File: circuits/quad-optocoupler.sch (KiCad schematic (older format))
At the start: 6 parts, among them U3 TLP291-4

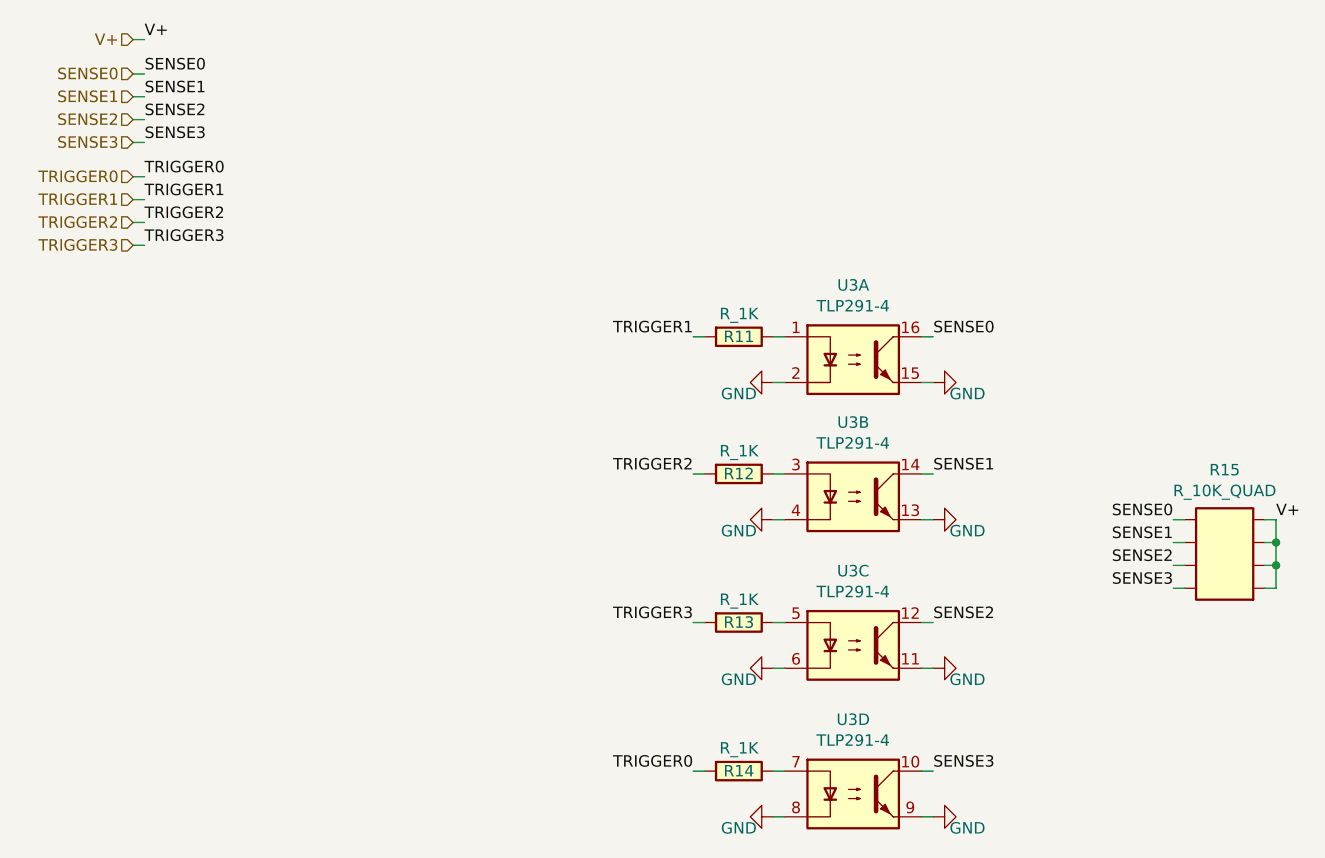
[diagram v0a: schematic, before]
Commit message: changed footprint for 0402 resistor array, sent back to fab
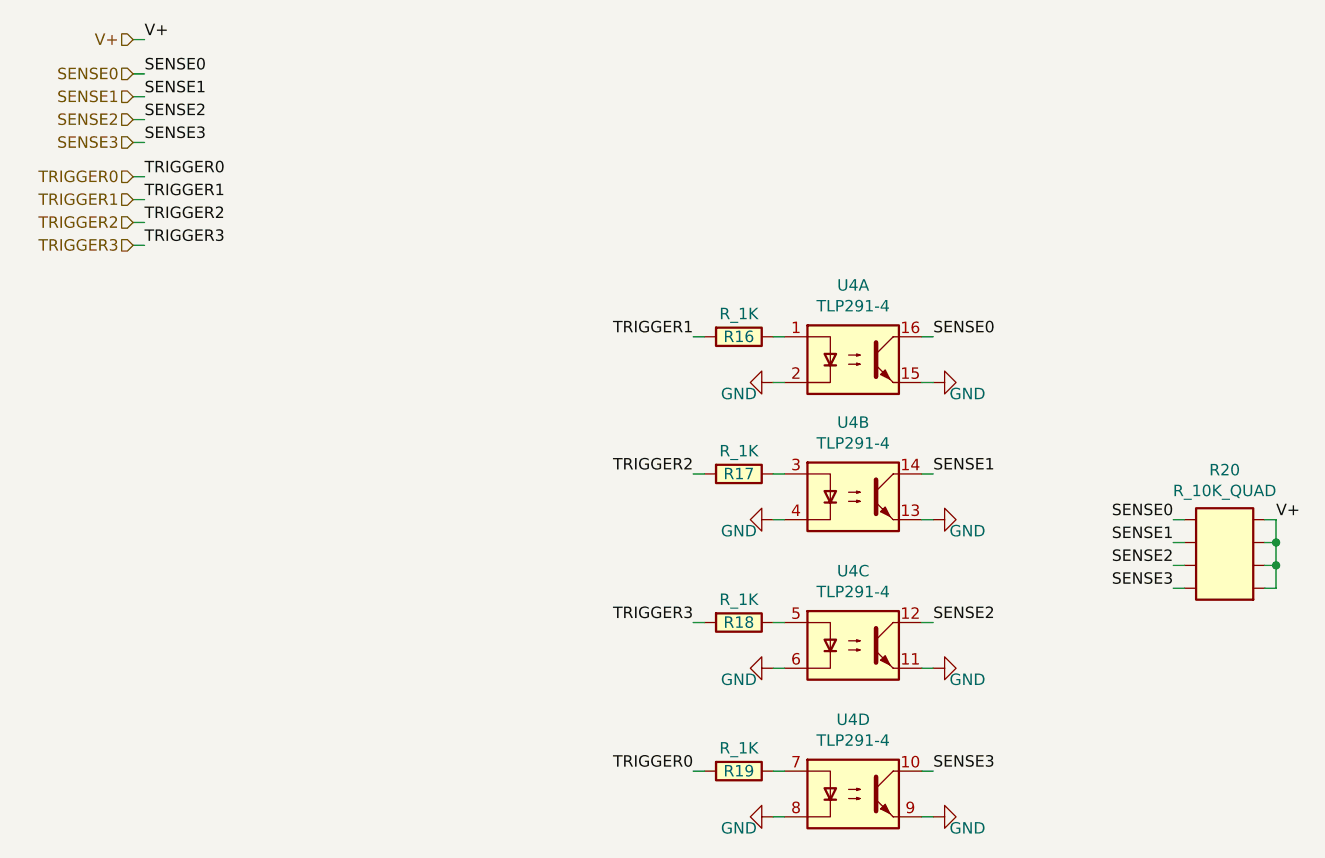
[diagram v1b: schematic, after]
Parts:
- R15: footprint Open_Automation:R_0402_1005Metric_Quad -> Resistor_SMD:R_Array_Concave_4x0402
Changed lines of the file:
@@
 $Descr A4 11693 8268
 encoding utf-8
-Sheet 4 12
+Sheet 5 12
 Title ""
 Date ""
@@
 AR Path="/601A4F03/5FDDC68F" Ref="U5"  Part="1"
 AR Path="/6021992A/5FDDC68F" Ref="U6"  Part="1"
-F 0 "U3" H 4350 2525 50  0000 C CNN
+F 0 "U4" H 4350 2525 50  0000 C CNN
 F 1 "TLP291-4" H 4350 2434 50  0000 C CNN
 F 2 "Package_SO:SOP-16_4.4x10.4mm_P1.27mm" H 4150 2000 50  0001 L CIN
@@
 AR Path="/601A4F03/5FDDC695" Ref="U5"  Part="2"
 AR Path="/6021992A/5FDDC695" Ref="U6"  Part="2"
-F 0 "U3" H 4350 3125 50  0000 C CNN
+F 0 "U4" H 4350 3125 50  0000 C CNN
 F 1 "TLP291-4" H 4350 3034 50  0000 C CNN
 F 2 "Package_SO:SOP-16_4.4x10.4mm_P1.27mm" H 4150 2600 50  0001 L CIN
@@
 AR Path="/601A4F03/5FDDC69B" Ref="U5"  Part="3"
 AR Path="/6021992A/5FDDC69B" Ref="U6"  Part="3"
-F 0 "U3" H 4350 3775 50  0000 C CNN
+F 0 "U4" H 4350 3775 50  0000 C CNN
 F 1 "TLP291-4" H 4350 3684 50  0000 C CNN
 F 2 "Package_SO:SOP-16_4.4x10.4mm_P1.27mm" H 4150 3250 50  0001 L CIN
@@
 AR Path="/601A4F03/5FDDC6A1" Ref="U5"  Part="4"
 AR Path="/6021992A/5FDDC6A1" Ref="U6"  Part="4"
-F 0 "U3" H 4350 4425 50  0000 C CNN
+F 0 "U4" H 4350 4425 50  0000 C CNN
 F 1 "TLP291-4" H 4350 4334 50  0000 C CNN
 F 2 "Package_SO:SOP-16_4.4x10.4mm_P1.27mm" H 4150 3900 50  0001 L CIN
@@
 AR Path="/601A4F03/5FF8C5A1" Ref="R25"  Part="1"
 AR Path="/6021992A/5FF8C5A1" Ref="R30"  Part="1"
-F 0 "R15" H 5975 3517 50  0000 C CNN
+F 0 "R20" H 5975 3517 50  0000 C CNN
 F 1 "R_10K_QUAD" H 5975 3426 50  0000 C CNN
-F 2 "Open_Automation:R_0402_1005Metric_Quad" H 6200 2500 50  0001 C CNN
+F 2 "Resistor_SMD:R_Array_Concave_4x0402" H 6200 2500 50  0001 C CNN
 F 3 "https://datasheet.lcsc.com/szlcsc/Uniroyal-Elec-4D02WGJ0103TCE_C25725.pdf" H 6200 2720 50  0001 C CNN
 F 4 "4D02WGJ0103TCE" H 6250 2670 60  0001 C CNN "Part Number"
@@
 AR Path="/601130DF/5FDC968D" Ref="#PWR042"  Part="1"
 AR Path="/6021992A/5FDC968D" Ref="#PWR058"  Part="1"
-F 0 "#PWR034" H 4700 2050 50  0001 C CNN
+F 0 "#PWR058" H 4700 2050 50  0001 C CNN
 F 1 "GND" V 4650 2150 50  0000 C CNN
 F 2 "" H 4700 2300 50  0001 C CNN
@@
 AR Path="/601130DF/5FDCB365" Ref="#PWR043"  Part="1"
 AR Path="/6021992A/5FDCB365" Ref="#PWR059"  Part="1"
-F 0 "#PWR035" H 4700 2650 50  0001 C CNN
+F 0 "#PWR059" H 4700 2650 50  0001 C CNN
 F 1 "GND" V 4650 2750 50  0000 C CNN
 F 2 "" H 4700 2900 50  0001 C CNN
@@
 AR Path="/601130DF/5FDCD5D6" Ref="#PWR044"  Part="1"
 AR Path="/6021992A/5FDCD5D6" Ref="#PWR060"  Part="1"
-F 0 "#PWR036" H 4700 3300 50  0001 C CNN
+F 0 "#PWR060" H 4700 3300 50  0001 C CNN
 F 1 "GND" V 4650 3400 50  0000 C CNN
 F 2 "" H 4700 3550 50  0001 C CNN
@@
 AR Path="/601130DF/5FDD131C" Ref="#PWR045"  Part="1"
 AR Path="/6021992A/5FDD131C" Ref="#PWR061"  Part="1"
-F 0 "#PWR037" H 4700 3950 50  0001 C CNN
+F 0 "#PWR061" H 4700 3950 50  0001 C CNN
 F 1 "GND" V 4650 4050 50  0000 C CNN
 F 2 "" H 4700 4200 50  0001 C CNN
@@
 AR Path="/601130DF/5FDD4573" Ref="#PWR041"  Part="1"
 AR Path="/6021992A/5FDD4573" Ref="#PWR057"  Part="1"
-F 0 "#PWR033" H 4000 3950 50  0001 C CNN
+F 0 "#PWR057" H 4000 3950 50  0001 C CNN
 F 1 "GND" V 4050 4050 50  0000 C CNN
 F 2 "" H 4000 4200 50  0001 C CNN
@@
 AR Path="/601130DF/5FDD7FBA" Ref="#PWR040"  Part="1"
 AR Path="/6021992A/5FDD7FBA" Ref="#PWR056"  Part="1"
-F 0 "#PWR032" H 4000 3300 50  0001 C CNN
+F 0 "#PWR056" H 4000 3300 50  0001 C CNN
 F 1 "GND" V 4050 3400 50  0000 C CNN
 F 2 "" H 4000 3550 50  0001 C CNN
@@
 AR Path="/601130DF/5FDDBD71" Ref="#PWR039"  Part="1"
 AR Path="/6021992A/5FDDBD71" Ref="#PWR055"  Part="1"
-F 0 "#PWR031" H 4000 2650 50  0001 C CNN
+F 0 "#PWR055" H 4000 2650 50  0001 C CNN
 F 1 "GND" V 4050 2750 50  0000 C CNN
 F 2 "" H 4000 2900 50  0001 C CNN
@@
 AR Path="/601130DF/5FDDF0DF" Ref="#PWR038"  Part="1"
 AR Path="/6021992A/5FDDF0DF" Ref="#PWR054"  Part="1"
-F 0 "#PWR030" H 4000 2050 50  0001 C CNN
+F 0 "#PWR054" H 4000 2050 50  0001 C CNN
 F 1 "GND" V 4050 2150 50  0000 C CNN
 F 2 "" H 4000 2300 50  0001 C CNN
@@
 AR Path="/601A4F03/5FDD0A2D" Ref="R21"  Part="1"
 AR Path="/6021992A/5FDD0A2D" Ref="R26"  Part="1"
-F 0 "R11" V 3850 2100 50  0000 C CNN
+F 0 "R16" V 3850 2100 50  0000 C CNN
 F 1 "R_1K" V 3750 2100 50  0000 C CNN
 F 2 "Resistor_SMD:R_0603_1608Metric_Pad0.98x0.95mm_HandSolder" V 3780 2100 50  0001 C CNN
@@
 AR Path="/601A4F03/5FDD4F3C" Ref="R22"  Part="1"
 AR Path="/6021992A/5FDD4F3C" Ref="R27"  Part="1"
-F 0 "R12" V 3850 2700 50  0000 C CNN
+F 0 "R17" V 3850 2700 50  0000 C CNN
 F 1 "R_1K" V 3750 2700 50  0000 C CNN
 F 2 "Resistor_SMD:R_0603_1608Metric_Pad0.98x0.95mm_HandSolder" V 3780 2700 50  0001 C CNN
@@
 AR Path="/601A4F03/5FDDB0BD" Ref="R23"  Part="1"
 AR Path="/6021992A/5FDDB0BD" Ref="R28"  Part="1"
-F 0 "R13" V 3850 3350 50  0000 C CNN
+F 0 "R18" V 3850 3350 50  0000 C CNN
 F 1 "R_1K" V 3750 3350 50  0000 C CNN
 F 2 "Resistor_SMD:R_0603_1608Metric_Pad0.98x0.95mm_HandSolder" V 3780 3350 50  0001 C CNN
@@
 AR Path="/601A4F03/5FDDEE05" Ref="R24"  Part="1"
 AR Path="/6021992A/5FDDEE05" Ref="R29"  Part="1"
-F 0 "R14" V 3850 4000 50  0000 C CNN
+F 0 "R19" V 3850 4000 50  0000 C CNN
 F 1 "R_1K" V 3750 4000 50  0000 C CNN
 F 2 "Resistor_SMD:R_0603_1608Metric_Pad0.98x0.95mm_HandSolder" V 3780 4000 50  0001 C CNN

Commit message: finished schematic corrections, working on layout
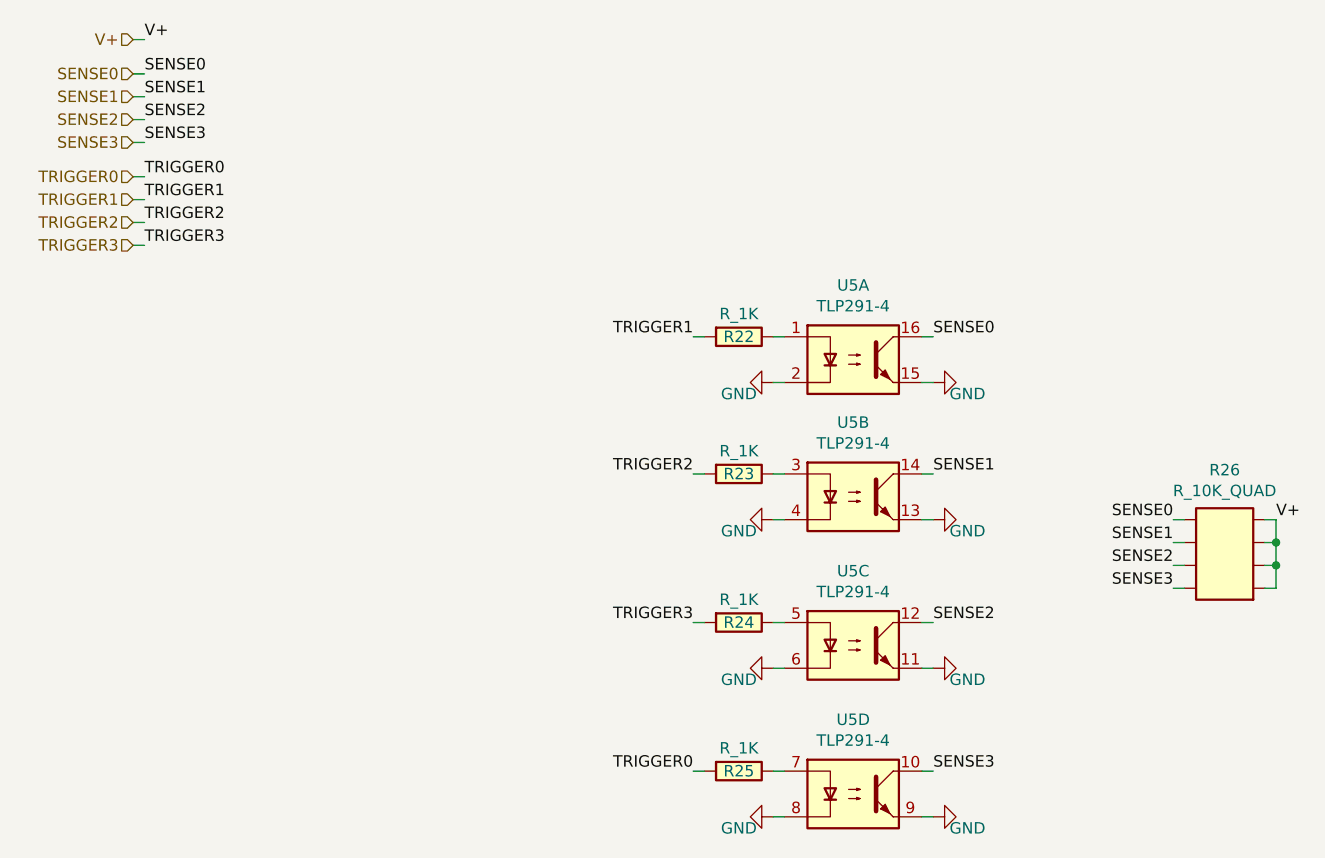
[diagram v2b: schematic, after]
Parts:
- renumbered R11 to R12, R12 to R13, R13 to R14, R14 to R15, R15 to R16

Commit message: finished layout, sent to board house
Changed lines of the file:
@@
 $Descr A4 11693 8268
 encoding utf-8
-Sheet 6 12
+Sheet 7 12
 Title ""
 Date ""
@@
 AR Path="/601A4F03/5FDDC68F" Ref="U5"  Part="1"
 AR Path="/6021992A/5FDDC68F" Ref="U6"  Part="1"
-F 0 "U5" H 4350 2525 50  0000 C CNN
+F 0 "U6" H 4350 2525 50  0000 C CNN
 F 1 "TLP291-4" H 4350 2434 50  0000 C CNN
 F 2 "Package_SO:SOP-16_4.4x10.4mm_P1.27mm" H 4150 2000 50  0001 L CIN
@@
 AR Path="/601A4F03/5FDDC695" Ref="U5"  Part="2"
 AR Path="/6021992A/5FDDC695" Ref="U6"  Part="2"
-F 0 "U5" H 4350 3125 50  0000 C CNN
+F 0 "U6" H 4350 3125 50  0000 C CNN
 F 1 "TLP291-4" H 4350 3034 50  0000 C CNN
 F 2 "Package_SO:SOP-16_4.4x10.4mm_P1.27mm" H 4150 2600 50  0001 L CIN
@@
 AR Path="/601A4F03/5FDDC69B" Ref="U5"  Part="3"
 AR Path="/6021992A/5FDDC69B" Ref="U6"  Part="3"
-F 0 "U5" H 4350 3775 50  0000 C CNN
+F 0 "U6" H 4350 3775 50  0000 C CNN
 F 1 "TLP291-4" H 4350 3684 50  0000 C CNN
 F 2 "Package_SO:SOP-16_4.4x10.4mm_P1.27mm" H 4150 3250 50  0001 L CIN
@@
 AR Path="/601A4F03/5FDDC6A1" Ref="U5"  Part="4"
 AR Path="/6021992A/5FDDC6A1" Ref="U6"  Part="4"
-F 0 "U5" H 4350 4425 50  0000 C CNN
+F 0 "U6" H 4350 4425 50  0000 C CNN
 F 1 "TLP291-4" H 4350 4334 50  0000 C CNN
 F 2 "Package_SO:SOP-16_4.4x10.4mm_P1.27mm" H 4150 3900 50  0001 L CIN
@@
 AR Path="/601A4F03/5FF8C5A1" Ref="R26"  Part="1"
 AR Path="/6021992A/5FF8C5A1" Ref="R31"  Part="1"
-F 0 "R26" H 5975 3517 50  0000 C CNN
+F 0 "R31" H 5975 3517 50  0000 C CNN
 F 1 "R_10K_QUAD" H 5975 3426 50  0000 C CNN
 F 2 "Resistor_SMD:R_Array_Concave_4x0402" H 6200 2500 50  0001 C CNN
@@
 AR Path="/601130DF/5FDC968D" Ref="#PWR041"  Part="1"
 AR Path="/6021992A/5FDC968D" Ref="#PWR057"  Part="1"
-F 0 "#PWR049" H 4700 2050 50  0001 C CNN
+F 0 "#PWR057" H 4700 2050 50  0001 C CNN
 F 1 "GND" V 4650 2150 50  0000 C CNN
 F 2 "" H 4700 2300 50  0001 C CNN
@@
 AR Path="/601130DF/5FDCB365" Ref="#PWR042"  Part="1"
 AR Path="/6021992A/5FDCB365" Ref="#PWR058"  Part="1"
-F 0 "#PWR050" H 4700 2650 50  0001 C CNN
+F 0 "#PWR058" H 4700 2650 50  0001 C CNN
 F 1 "GND" V 4650 2750 50  0000 C CNN
 F 2 "" H 4700 2900 50  0001 C CNN
@@
 AR Path="/601130DF/5FDCD5D6" Ref="#PWR043"  Part="1"
 AR Path="/6021992A/5FDCD5D6" Ref="#PWR059"  Part="1"
-F 0 "#PWR051" H 4700 3300 50  0001 C CNN
+F 0 "#PWR059" H 4700 3300 50  0001 C CNN
 F 1 "GND" V 4650 3400 50  0000 C CNN
 F 2 "" H 4700 3550 50  0001 C CNN
@@
 AR Path="/601130DF/5FDD131C" Ref="#PWR044"  Part="1"
 AR Path="/6021992A/5FDD131C" Ref="#PWR060"  Part="1"
-F 0 "#PWR052" H 4700 3950 50  0001 C CNN
+F 0 "#PWR060" H 4700 3950 50  0001 C CNN
 F 1 "GND" V 4650 4050 50  0000 C CNN
 F 2 "" H 4700 4200 50  0001 C CNN
@@
 AR Path="/601130DF/5FDD4573" Ref="#PWR040"  Part="1"
 AR Path="/6021992A/5FDD4573" Ref="#PWR056"  Part="1"
-F 0 "#PWR048" H 4000 3950 50  0001 C CNN
+F 0 "#PWR056" H 4000 3950 50  0001 C CNN
 F 1 "GND" V 4050 4050 50  0000 C CNN
 F 2 "" H 4000 4200 50  0001 C CNN
@@
 AR Path="/601130DF/5FDD7FBA" Ref="#PWR039"  Part="1"
 AR Path="/6021992A/5FDD7FBA" Ref="#PWR055"  Part="1"
-F 0 "#PWR047" H 4000 3300 50  0001 C CNN
+F 0 "#PWR055" H 4000 3300 50  0001 C CNN
 F 1 "GND" V 4050 3400 50  0000 C CNN
 F 2 "" H 4000 3550 50  0001 C CNN
@@
 AR Path="/601130DF/5FDDBD71" Ref="#PWR038"  Part="1"
 AR Path="/6021992A/5FDDBD71" Ref="#PWR054"  Part="1"
-F 0 "#PWR046" H 4000 2650 50  0001 C CNN
+F 0 "#PWR054" H 4000 2650 50  0001 C CNN
 F 1 "GND" V 4050 2750 50  0000 C CNN
 F 2 "" H 4000 2900 50  0001 C CNN
@@
 AR Path="/601130DF/5FDDF0DF" Ref="#PWR037"  Part="1"
 AR Path="/6021992A/5FDDF0DF" Ref="#PWR053"  Part="1"
-F 0 "#PWR045" H 4000 2050 50  0001 C CNN
+F 0 "#PWR053" H 4000 2050 50  0001 C CNN
 F 1 "GND" V 4050 2150 50  0000 C CNN
 F 2 "" H 4000 2300 50  0001 C CNN
@@
 AR Path="/601A4F03/5FDD0A2D" Ref="R22"  Part="1"
 AR Path="/6021992A/5FDD0A2D" Ref="R27"  Part="1"
-F 0 "R22" V 3850 2100 50  0000 C CNN
+F 0 "R27" V 3850 2100 50  0000 C CNN
 F 1 "R_1K" V 3750 2100 50  0000 C CNN
 F 2 "Resistor_SMD:R_0603_1608Metric_Pad0.98x0.95mm_HandSolder" V 3780 2100 50  0001 C CNN
@@
 AR Path="/601A4F03/5FDD4F3C" Ref="R23"  Part="1"
 AR Path="/6021992A/5FDD4F3C" Ref="R28"  Part="1"
-F 0 "R23" V 3850 2700 50  0000 C CNN
+F 0 "R28" V 3850 2700 50  0000 C CNN
 F 1 "R_1K" V 3750 2700 50  0000 C CNN
 F 2 "Resistor_SMD:R_0603_1608Metric_Pad0.98x0.95mm_HandSolder" V 3780 2700 50  0001 C CNN
@@
 AR Path="/601A4F03/5FDDB0BD" Ref="R24"  Part="1"
 AR Path="/6021992A/5FDDB0BD" Ref="R29"  Part="1"
-F 0 "R24" V 3850 3350 50  0000 C CNN
+F 0 "R29" V 3850 3350 50  0000 C CNN
 F 1 "R_1K" V 3750 3350 50  0000 C CNN
 F 2 "Resistor_SMD:R_0603_1608Metric_Pad0.98x0.95mm_HandSolder" V 3780 3350 50  0001 C CNN
@@
 AR Path="/601A4F03/5FDDEE05" Ref="R25"  Part="1"
 AR Path="/6021992A/5FDDEE05" Ref="R30"  Part="1"
-F 0 "R25" V 3850 4000 50  0000 C CNN
+F 0 "R30" V 3850 4000 50  0000 C CNN
 F 1 "R_1K" V 3750 4000 50  0000 C CNN
 F 2 "Resistor_SMD:R_0603_1608Metric_Pad0.98x0.95mm_HandSolder" V 3780 4000 50  0001 C CNN
